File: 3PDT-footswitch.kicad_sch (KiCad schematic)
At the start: 14 parts

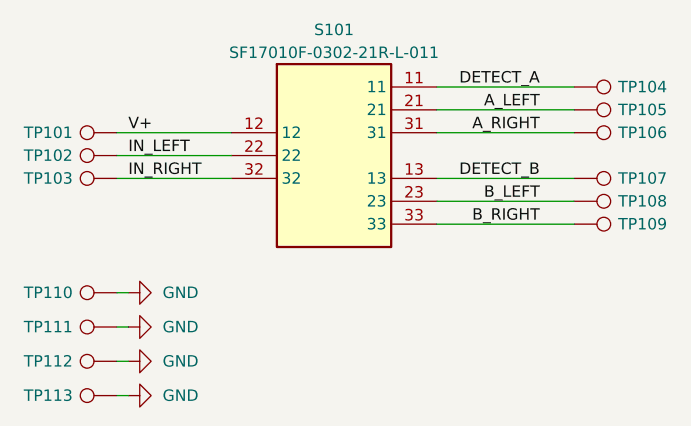
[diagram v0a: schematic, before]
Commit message: smaller pcb, added silkscreens
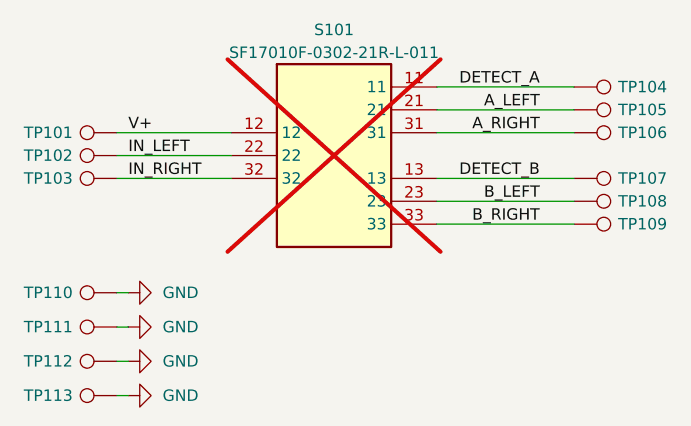
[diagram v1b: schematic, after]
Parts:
- S101: now not fitted
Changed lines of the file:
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@@
 		(in_bom yes)
 		(on_board yes)
-		(dnp no)
+		(dnp yes)
 		(property "Reference" "S101"
 			(at 152.4 26.67 0)
